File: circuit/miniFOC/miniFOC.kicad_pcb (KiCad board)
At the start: 2 copper layers, 68 parts, among them J1 Conn_01x05, J2 Conn_01x06, J3 Conn_01x02, J4 Conn_01x01, J5 Conn_01x01, J6 Conn_01x01, Q1 AP30H50Q, Q2 AP30H50Q, Q3 AP30H50Q, Q4 AP30H50Q, Q5 AP30H50Q, Q6 AP30H50Q, U1 XC6206P332MR, U2 AT32F421C8, U3 LM321, U4 COS722MR, U5 EG2133, U6 JW5017S

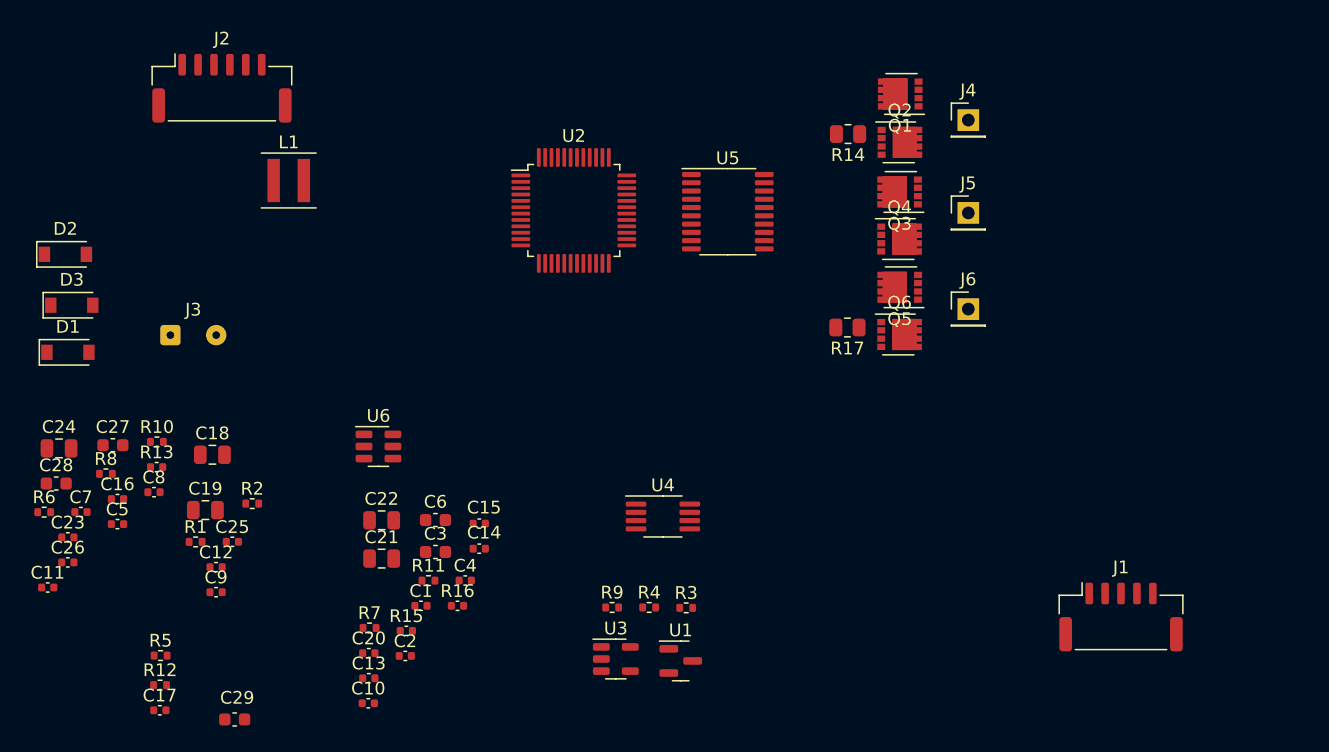
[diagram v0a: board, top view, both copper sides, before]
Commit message: Complete the circuit and PCB design for version 2.0.
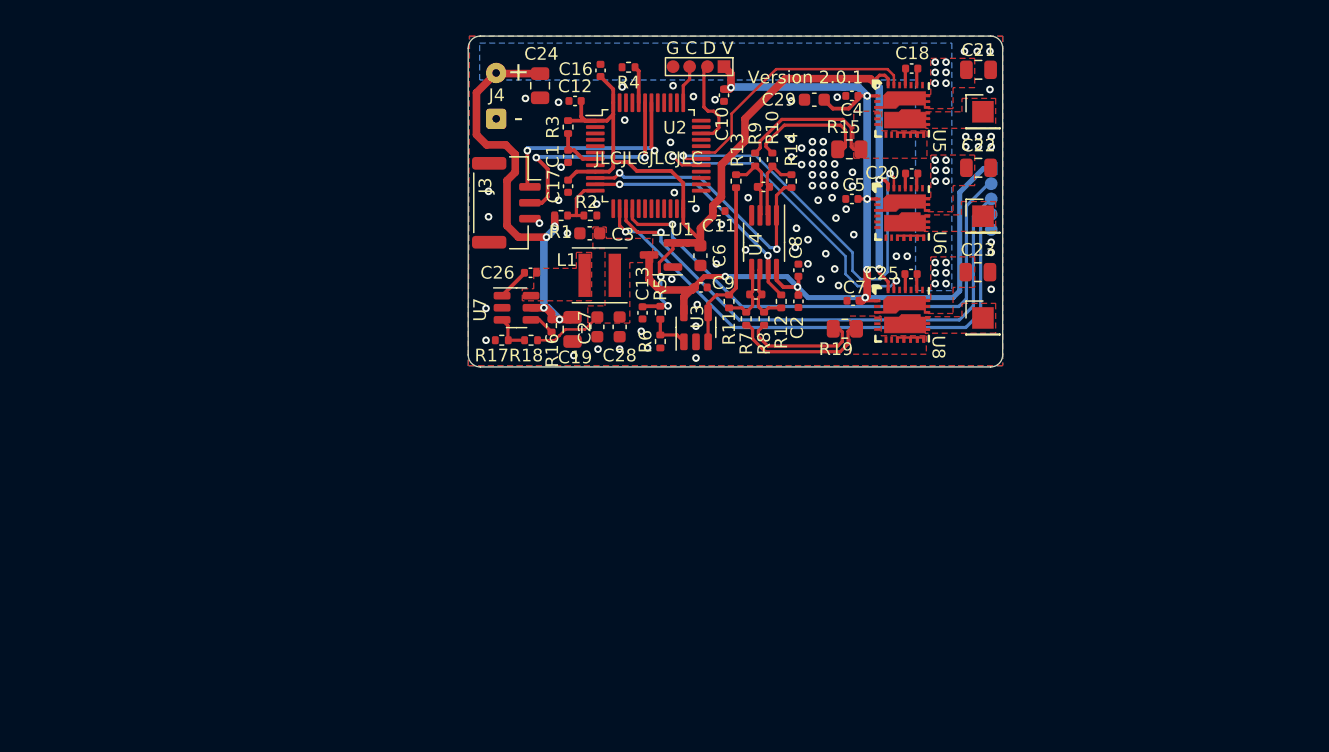
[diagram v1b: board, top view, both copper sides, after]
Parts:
- removed the C23 at (101.2, 131.0)
- removed D1, D2, D3: B0530W, Diode_SMD:D_SOD-123
- removed Q1, Q2, Q3, Q4, Q5, Q6: AP30H50Q, Package_SON:VSON-8_3.3x3.3mm_P0.65mm_NexFET
- added C20: 1uF, Library:C_0402_1005Metric, F.Cu at (167.6, 102.4)
- added G***: LOGO, Library:LOGO, B.Cu at (139.2, 106.3)
- added J3: Conn_01x03, Library:JST_GH_SM03B-GHS-TB_1x03-1MP_P1.25mm_Horizontal, F.Cu at (135.7, 104.7)
- added R1: 1kR, Library:R_0402_1005Metric, F.Cu at (140.0, 105.7)
- added R2: 1kR, Library:R_0402_1005Metric, F.Cu at (142.3, 105.7)
- added U6: uP9636, Library:QFN-26_4040_IPS, F.Cu at (166.8, 105.5)
- added U8: uP9636, Library:QFN-26_4040_IPS, F.Cu at (166.8, 113.5)
- C1, C10, C11, C12, C13, C14, C15, C16, C17, C2, C25, C26, C4, C5, C7, C8, C9: footprint Capacitor_SMD:C_0402_1005Metric -> Library:C_0402_1005Metric
- C18: renamed from C20; footprint Capacitor_SMD:C_0402_1005Metric -> Library:C_0402_1005Metric
- C19: renamed from C18; footprint Capacitor_SMD:C_0805_2012Metric -> Library:C_0805_2012Metric
- C21: renamed from C19; footprint Capacitor_SMD:C_0805_2012Metric -> Library:C_0805_2012Metric
- C22: renamed from C21; footprint Capacitor_SMD:C_0805_2012Metric -> Library:C_0805_2012Metric
- C23: renamed from C22; footprint Capacitor_SMD:C_0805_2012Metric -> Library:C_0805_2012Metric
- C24: footprint Capacitor_SMD:C_0805_2012Metric -> Library:C_0805_2012Metric
- C27, C28, C29: footprint Capacitor_SMD:C_0603_1608Metric -> Library:C_0603_1608Metric
- C3, C6: value 10uF -> 22uF; footprint Capacitor_SMD:C_0603_1608Metric -> Library:C_0603_1608Metric
- J1: footprint Connector_JST:JST_GH_SM05B-GHS-TB_1x05-1MP_P1.25mm_Horizontal -> Library:Pad_5; moved to B.Cu
- J2: value Conn_01x06 -> Conn_01x04; footprint Connector_JST:JST_GH_SM06B-GHS-TB_1x06-1MP_P1.25mm_Horizontal -> Library:Pad_4
- J4: renamed from J3; footprint Connector_Wire:SolderWire-0.1sqmm_1x02_P3.6mm_D0.4mm_OD1mm -> Library:SolderWire-0.1sqmm_1x02_P3.6mm_D0.4mm_OD1mm
- J5: renamed from J4; footprint Connector_PinHeader_2.54mm:PinHeader_1x01_P2.54mm_Vertical -> Library:Pad_1
- J6: renamed from J5; footprint Connector_PinHeader_2.54mm:PinHeader_1x01_P2.54mm_Vertical -> Library:Pad_1
- J7: renamed from J6; footprint Connector_PinHeader_2.54mm:PinHeader_1x01_P2.54mm_Vertical -> Library:Pad_1
- L1: footprint Inductor_SMD:L_Coilcraft_XxL4040 -> Library:L_Coilcraft_XxL4040
- R10: renamed from R8; footprint Resistor_SMD:R_0402_1005Metric -> Library:R_0402_1005Metric
- R11: renamed from R9; footprint Resistor_SMD:R_0402_1005Metric -> Library:R_0402_1005Metric
- R12: renamed from R10; footprint Resistor_SMD:R_0402_1005Metric -> Library:R_0402_1005Metric
- R13: renamed from R11; footprint Resistor_SMD:R_0402_1005Metric -> Library:R_0402_1005Metric
- R14: renamed from R12; footprint Resistor_SMD:R_0402_1005Metric -> Library:R_0402_1005Metric
- R15: renamed from R14; footprint Resistor_SMD:R_0805_2012Metric -> Library:R_0805_2012Metric
- R16: renamed from R13; footprint Capacitor_SMD:C_0402_1005Metric -> Library:R_0402_1005Metric
- R17: renamed from R15; footprint Capacitor_SMD:C_0402_1005Metric -> Library:R_0402_1005Metric
- R18: renamed from R16; footprint Capacitor_SMD:C_0402_1005Metric -> Library:R_0402_1005Metric
- R19: renamed from R17; footprint Resistor_SMD:R_0805_2012Metric -> Library:R_0805_2012Metric
- R3: renamed from R1; footprint Resistor_SMD:R_0402_1005Metric -> Library:R_0402_1005Metric
- R4: renamed from R2; footprint Resistor_SMD:R_0402_1005Metric -> Library:R_0402_1005Metric
- R5: renamed from R3; footprint Resistor_SMD:R_0402_1005Metric -> Library:R_0402_1005Metric
- R6: renamed from R4; footprint Resistor_SMD:R_0402_1005Metric -> Library:R_0402_1005Metric
- R7: renamed from R5; footprint Resistor_SMD:R_0402_1005Metric -> Library:R_0402_1005Metric
- R8: renamed from R6; footprint Resistor_SMD:R_0402_1005Metric -> Library:R_0402_1005Metric
- R9: renamed from R7; footprint Resistor_SMD:R_0402_1005Metric -> Library:R_0402_1005Metric
- U1: footprint Package_TO_SOT_SMD:SOT-23 -> Library:SOT-23
- U2: footprint Package_QFP:LQFP-48_7x7mm_P0.5mm -> Library:LQFP-48_7x7mm_P0.5mm
- U3: footprint Package_TO_SOT_SMD:SOT-23-5 -> Library:SOT-23-5
- U4: footprint Package_SO:MSOP-8_3x3mm_P0.65mm -> Library:MSOP-8_3x3mm_P0.65mm
- U5: value EG2133 -> uP9636; footprint Package_SO:TSSOP-20_4.4x6.5mm_P0.65mm -> Library:QFN-26_4040_IPS
- U7: renamed from U6; footprint Package_TO_SOT_SMD:SOT-23-6 -> Library:SOT-23-6
- moved C21 69.9 mm to (172.8, 94.2), turned to 180 degrees
- moved C29 66.7 mm to (159.9, 96.6)
- moved R14 63.5 mm to (158.1, 103.0), turned to -90 degrees
- moved C5 63.1 mm to (162.8, 104.4), turned to 180 degrees
- moved C7 62.9 mm to (162.9, 112.4), turned to 180 degrees
- moved C18 62.7 mm to (167.6, 94.2)
- moved C11 60.5 mm to (152.4, 105.3)
- moved R8 58.6 mm to (155.9, 113.8), turned to -90 degrees
- moved R10 57.9 mm to (156.6, 101.3), turned to 90 degrees
- moved C25 57.3 mm to (167.5, 110.3)
- moved C22 56.1 mm to (172.8, 102.0), turned to 180 degrees
- moved C10 55.4 mm to (152.8, 96.2), turned to -90 degrees
- moved C8 53.6 mm to (158.7, 110.0), turned to 90 degrees
- moved R7 53.1 mm to (154.6, 113.8), turned to 90 degrees
- moved C17 52.2 mm to (140.6, 103.4), turned to -90 degrees
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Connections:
- C18 pad 1: /VB1 -> Net-(C18-Pad1)
- C18 pad 2: /VS1 -> Net-(C18-Pad2)
- C25 pad 1: /VB3 -> Net-(C25-Pad1)
- C25 pad 2: /VS3 -> Net-(C25-Pad2)
- J2 pad 2: /USART1_TX -> /SWDIO
- J2 pad 3: /USART1_RX -> /SWDCLK
- J2 pad 4: /SWDIO -> GND
- J5 pad 1: /VS1 -> Net-(J5-Pad1)
- J6 pad 1: /VS2 -> Net-(J6-Pad1)
- J7 pad 1: /VS3 -> Net-(J7-Pad1)
- U5 pad 1: /TIM1_CH3 -> +5V
- U5 pad 2: /TIM1_CH2 -> unconnected-(U5-Pad2)
- U5 pad 20: /VB1 -> unconnected-(U5-Pad20)
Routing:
- net +5V: track 0.00 -> 90.1 mm, vias 0 -> 7
- net +3.3V: track 0.00 -> 82.5 mm, vias 0 -> 5
- net /SPI_CS: track 0.00 -> 41.6 mm, vias 0 -> 1
- net /SPI_CLK: track 0.00 -> 41.4 mm, vias 0 -> 1
- net /SPI_MISO: track 0.00 -> 40.7 mm, vias 0 -> 1
- net +15V: track 0.00 -> 35.2 mm, vias 0 -> 22
- net /TIM1_CH2: track 0.00 -> 31.8 mm, vias 0 -> 2
- net /TIM1_CH1: track 0.00 -> 26.1 mm, vias 0 -> 2
- net /ADC1_CH0: track 0.00 -> 22.6 mm, vias 0 -> 2
- net /TIM1_CH3: track 0.00 -> 19.8 mm
- net GND: track 0.00 -> 19.7 mm, vias 0 -> 81
- net /ADC1_CH1: track 0.00 -> 19.4 mm, vias 0 -> 2
- net /USART1_RX: track 0.00 -> 18.0 mm, vias 0 -> 2
- net /USART1_TX: track 0.00 -> 17.1 mm, vias 0 -> 2
- net VAA: track 0.00 -> 13.6 mm
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- added copper zone on B.Cu, net +15V
- added copper zone on F.Cu, net +15V
- added copper zone on F.Cu, net +5V
- added copper zone on F.Cu, net /SA1_P
- added copper zone on F.Cu, net /SA2_P
- added copper zone on B.Cu, net GND
- added copper zone on F.Cu, net GND
- added copper zone on F.Cu, net Net-(C26-Pad1)
- added copper zone on F.Cu, net Net-(J5-Pad1)
- added copper zone on F.Cu, net Net-(J6-Pad1)
- added copper zone on F.Cu, net Net-(J7-Pad1)
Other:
- board outline added: 42 x 26 mm
- board text added: "+"
- board text added: "-"
- board text added: "0"
- board text added: "0 mm"
- board text added: "0.01 mm"
- board text added: "0.02"
- board text added: "0.035 mm"
- board text added: "0.2000 mm / 0.2000 mm"
- board text added: "0.3000 mm"
- board text added: "1"
- board text added: "1.51 mm"
- board text added: "1.6000 mm"
- board text added: "2"
- board text added: "3.3"
- board text added: "4.5"
- board text added: "42.0000 mm x 26.0000 mm"
- board text added: "B.Cu"
- board text added: "B.Mask"
- board text added: "B.Paste"
- board text added: "B.Silkscreen"
- board text added: "BOARD CHARACTERISTICS"
- board text added: "Black"
- board text added: "Bottom Silk Screen"
- board text added: "Bottom Solder Mask"
- board text added: "Bottom Solder Paste"
- board text added: "Epsilon R（相对介电常数）"
- board text added: "F.Cu"
- board text added: "F.Mask"
- board text added: "F.Paste"
- board text added: "F.Silkscreen"
- board text added: "FR4"
- board text added: "G C D V"
- board text added: "JLCJLCJLCJLC"
- board text added: "Loss Tangent（损耗角正切）"
- board text added: "None"
- board text added: "Not specified"
- board text added: "Top Silk Screen"
- board text added: "Top Solder Mask"
- board text added: "Top Solder Paste"
- board text added: "V I C E G"
- board text added: "Version 2.0.1"
- board text added: "White"
- board text added: "copper"
- board text added: "core"
- board text added: "github.com/zhuyanzhen1/miniFOC"
- board text added: "miniFOC"
- board text added: "否"
- board text added: "孔最小直径："
- board text added: "层名称"
- board text added: "最小布线/间距："
- board text added: "材料"
- board text added: "板子整体尺寸："
- board text added: "电介质层 1"
- board text added: "电路板厚度："
- board text added: "电镀板边："
- board text added: "类型"
- board text added: "粗细 (mm)"
- board text added: "边缘卡连接器："
- board text added: "邮票孔："
- board text added: "铜层数量："
- board text added: "铜表面处理（镀铜）："
- board text added: "阻抗控制"
- board text added: "颜色"

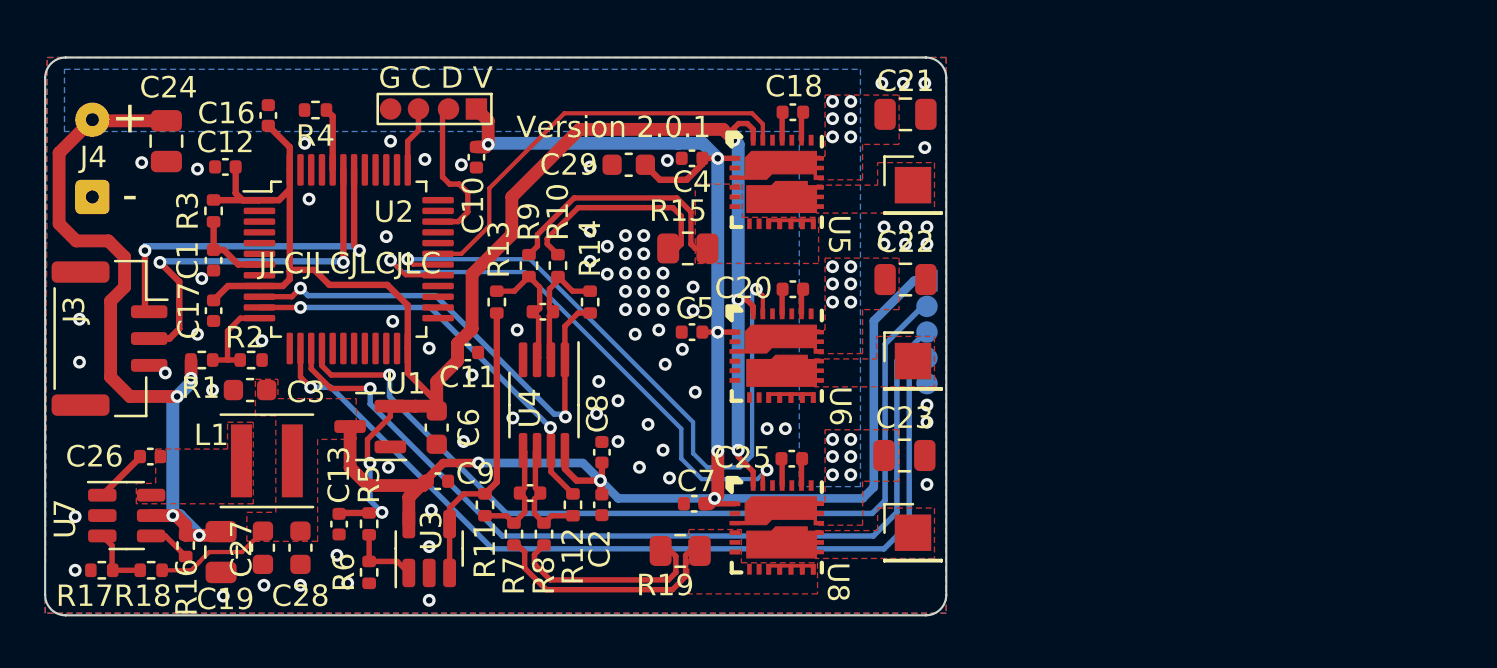
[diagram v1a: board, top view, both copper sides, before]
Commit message: Mosify miniFOC schematic, using new scheme
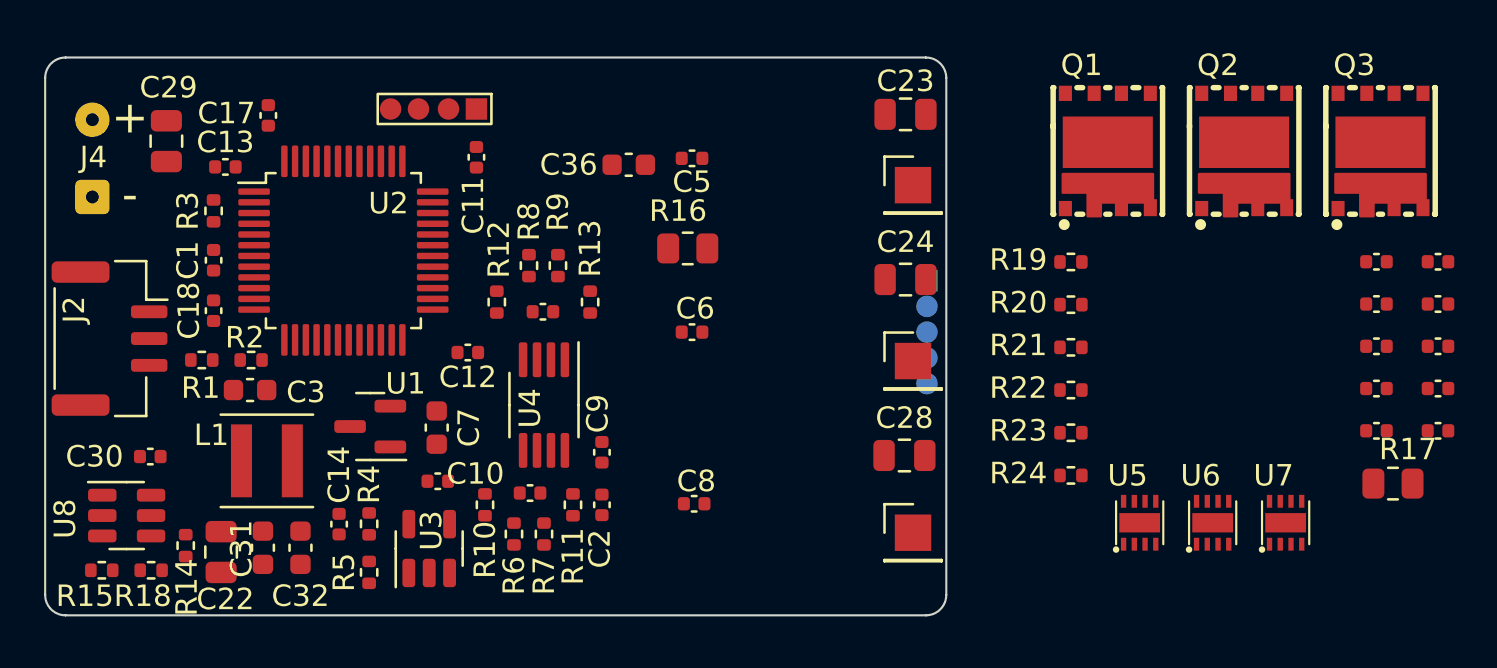
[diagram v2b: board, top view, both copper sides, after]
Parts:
- removed the C18 at (167.6, 94.2)
- removed G***: LOGO, Library:LOGO
- removed the R4 at (145.3, 94.0)
- removed the U8 at (166.8, 113.5)
- added C19: 100nF, library:C_0402_1005Metric, F.Cu at (194.8, 103.1)
- added C21: 100nF, library:C_0402_1005Metric, F.Cu at (194.8, 107.0)
- added C26: 1uF, library:C_0402_1005Metric, F.Cu at (197.6, 101.1)
- added C27: 1uF, library:C_0402_1005Metric, F.Cu at (197.6, 103.1)
- added C33: 1uF, library:C_0402_1005Metric, F.Cu at (197.6, 105.1)
- added C34: 1uF, library:C_0402_1005Metric, F.Cu at (197.6, 107.0)
- added C35: 1uF, library:C_0402_1005Metric, F.Cu at (197.6, 109.0)
- added C4: 1uF, library:C_0402_1005Metric, F.Cu at (194.8, 101.1)
- added Q1: RU30J30M, library:PDFN-8_L5.8-W4.9_RU30J30M, F.Cu at (182.2, 96.0)
- added Q2: RU30J30M, library:PDFN-8_L5.8-W4.9_RU30J30M, F.Cu at (188.6, 96.0)
- added Q3: RU30J30M, library:PDFN-8_L5.8-W4.9_RU30J30M, F.Cu at (194.9, 96.0)
- added R17: 20mR, library:R_0805_2012Metric, F.Cu at (195.5, 111.5)
- added R20: 1kR, library:R_0402_1005Metric, F.Cu at (180.5, 103.1)
- added R21: 10kR, library:R_0402_1005Metric, F.Cu at (180.5, 105.1)
- added R22: 1kR, library:R_0402_1005Metric, F.Cu at (180.5, 107.1)
- added R23: 10kR, library:R_0402_1005Metric, F.Cu at (180.5, 109.1)
- added R24: 1kR, library:R_0402_1005Metric, F.Cu at (180.5, 111.1)
- added U7: BDR2L00, library:TDFN-8_L2.0-W2.0-P0.50-BL-EP, F.Cu at (190.5, 113.3)
- C1, C2, C25: footprint Library:C_0402_1005Metric -> library:C_0402_1005Metric
- C10: renamed from C9; footprint Library:C_0402_1005Metric -> library:C_0402_1005Metric
- C11: renamed from C10; footprint Library:C_0402_1005Metric -> library:C_0402_1005Metric
- C12: renamed from C11; footprint Library:C_0402_1005Metric -> library:C_0402_1005Metric
- C13: renamed from C12; footprint Library:C_0402_1005Metric -> library:C_0402_1005Metric
- C14: renamed from C13; footprint Library:C_0402_1005Metric -> library:C_0402_1005Metric
- C15: renamed from C14; footprint Library:C_0402_1005Metric -> library:C_0402_1005Metric
- C16: renamed from C15; footprint Library:C_0402_1005Metric -> library:C_0402_1005Metric
- C17: renamed from C16; footprint Library:C_0402_1005Metric -> library:C_0402_1005Metric
- C18: renamed from C17; footprint Library:C_0402_1005Metric -> library:C_0402_1005Metric
- C20: value 1uF -> 100nF; footprint Library:C_0402_1005Metric -> library:C_0402_1005Metric
- C22: renamed from C19; footprint Library:C_0805_2012Metric -> library:C_0805_2012Metric
- C23: renamed from C21; footprint Library:C_0805_2012Metric -> library:C_0805_2012Metric
- C24: renamed from C22; footprint Library:C_0805_2012Metric -> library:C_0805_2012Metric
- C28: renamed from C23; footprint Library:C_0805_2012Metric -> library:C_0805_2012Metric
- C29: renamed from C24; footprint Library:C_0805_2012Metric -> library:C_0805_2012Metric
- C3: footprint Library:C_0603_1608Metric -> library:C_0603_1608Metric
- C30: renamed from C26; footprint Library:C_0402_1005Metric -> library:C_0402_1005Metric
- C31: renamed from C27; footprint Library:C_0603_1608Metric -> library:C_0603_1608Metric
- C32: renamed from C28; footprint Library:C_0603_1608Metric -> library:C_0603_1608Metric
- C36: renamed from C29; footprint Library:C_0603_1608Metric -> library:C_0603_1608Metric
- C5: renamed from C4; footprint Library:C_0402_1005Metric -> library:C_0402_1005Metric
- C6: renamed from C5; footprint Library:C_0402_1005Metric -> library:C_0402_1005Metric
- C7: renamed from C6; footprint Library:C_0603_1608Metric -> library:C_0603_1608Metric
- C8: renamed from C7; footprint Library:C_0402_1005Metric -> library:C_0402_1005Metric
- C9: renamed from C8; footprint Library:C_0402_1005Metric -> library:C_0402_1005Metric
- J1: footprint Library:Pad_5 -> library:Pad_5
- J2: renamed from J3; footprint Library:JST_GH_SM03B-GHS-TB_1x03-1MP_P1.25mm_Horizontal -> library:JST_GH_SM03B-GHS-TB_1x03-1MP_P1.25mm_Horizontal
- J3: renamed from J2; footprint Library:Pad_4 -> library:Pad_4
- J4: footprint Library:SolderWire-0.1sqmm_1x02_P3.6mm_D0.4mm_OD1mm -> library:SolderWire-0.1sqmm_1x02_P3.6mm_D0.4mm_OD1mm
- J5, J6, J7: footprint Library:Pad_1 -> library:Pad_1
- L1: footprint Library:L_Coilcraft_XxL4040 -> library:L_Coilcraft_XxL4040
- R1: value 1kR -> 10kR; footprint Library:R_0402_1005Metric -> library:R_0402_1005Metric
- R10: renamed from R11; footprint Library:R_0402_1005Metric -> library:R_0402_1005Metric
- R11: renamed from R12; footprint Library:R_0402_1005Metric -> library:R_0402_1005Metric
- R12: renamed from R13; footprint Library:R_0402_1005Metric -> library:R_0402_1005Metric
- R13: renamed from R14; footprint Library:R_0402_1005Metric -> library:R_0402_1005Metric
- R14: renamed from R16; footprint Library:R_0402_1005Metric -> library:R_0402_1005Metric
- R15: renamed from R17; footprint Library:R_0402_1005Metric -> library:R_0402_1005Metric
- R16: renamed from R15; footprint Library:R_0805_2012Metric -> library:R_0805_2012Metric
- R18, R2, R3: footprint Library:R_0402_1005Metric -> library:R_0402_1005Metric
- R19: value 20mR -> 10kR; footprint Library:R_0805_2012Metric -> library:R_0402_1005Metric
- R4: renamed from R5; footprint Library:R_0402_1005Metric -> library:R_0402_1005Metric
- R5: renamed from R6; footprint Library:R_0402_1005Metric -> library:R_0402_1005Metric
- R6: renamed from R7; footprint Library:R_0402_1005Metric -> library:R_0402_1005Metric
- R7: renamed from R8; footprint Library:R_0402_1005Metric -> library:R_0402_1005Metric
- R8: renamed from R9; footprint Library:R_0402_1005Metric -> library:R_0402_1005Metric
- R9: renamed from R10; footprint Library:R_0402_1005Metric -> library:R_0402_1005Metric
- U1: footprint Library:SOT-23 -> library:SOT-23
- U2: value AT32F421C8 -> CH32V203C8T6; footprint Library:LQFP-48_7x7mm_P0.5mm -> library:LQFP-48_7x7mm_P0.5mm
- U3: footprint Library:SOT-23-5 -> library:SOT-23-5
- U4: footprint Library:MSOP-8_3x3mm_P0.65mm -> library:MSOP-8_3x3mm_P0.65mm
- U5, U6: value uP9636 -> BDR2L00; footprint Library:QFN-26_4040_IPS -> library:TDFN-8_L2.0-W2.0-P0.50-BL-EP
- U8: renamed from U7; footprint Library:SOT-23-6 -> library:SOT-23-6
- moved C20 27.3 mm to (194.8, 105.1)
- moved C25 27.3 mm to (194.8, 109.0)
- moved U5 23.2 mm to (183.7, 113.3), turned to 0 degrees
- moved R19 22.7 mm to (180.5, 101.1), turned to 0 degrees
- moved U6 21.8 mm to (187.1, 113.3), turned to 0 degrees
- moved U2 0.47 mm to (146.6, 100.6)
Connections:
- C20 pad 1: Net-(C20-Pad1) -> +5V
- C20 pad 2: Net-(C20-Pad2) -> GND
- C25 pad 1: Net-(C25-Pad1) -> Net-(U5-BOOT)
- C25 pad 2: Net-(C25-Pad2) -> /PHASE1
- J5 pad 1: Net-(J5-Pad1) -> /PHASE1
- J6 pad 1: Net-(J6-Pad1) -> /PHASE2
- J7 pad 1: Net-(J7-Pad1) -> /PHASE3
- R19 pad 1: /SA2_P -> /PHASE1
- R19 pad 2: GND -> /ADC_U
- U2 pad 13: unconnected-(U2-Pad13) -> /ADC_U
- U2 pad 14: /SPI_CS -> /ADC_V
- U2 pad 15: /SPI_CLK -> /ADC_W
- U2 pad 16: /SPI_MISO -> unconnected-(U2-PA6-Pad16)
- U2 pad 25: unconnected-(U2-Pad25) -> /SPI_CS
- U2 pad 26: unconnected-(U2-Pad26) -> /SPI_CLK
- U2 pad 27: unconnected-(U2-Pad27) -> /SPI_MISO
- U2 pad 44: /BOOT0 -> GND
- U5 pad 1: +5V -> Net-(U5-BOOT)
- U5 pad 2: unconnected-(U5-Pad2) -> /TIM1_CH1
- U6 pad 1: +5V -> Net-(U6-BOOT)
- U6 pad 2: unconnected-(U6-Pad2) -> /TIM1_CH2
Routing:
- net +5V: track 90.1 -> 0.00 mm, vias 7 -> 0
- net +3.3V: track 82.5 -> 0.00 mm, vias 5 -> 0
- net /SPI_CS: track 41.6 -> 0.00 mm, vias 1 -> 0
- net /SPI_CLK: track 41.4 -> 0.00 mm, vias 1 -> 0
- net /SPI_MISO: track 40.7 -> 0.00 mm, vias 1 -> 0
- net +15V: track 35.2 -> 0.00 mm, vias 22 -> 0
- net /TIM1_CH2: track 31.8 -> 0.00 mm, vias 2 -> 0
- net /TIM1_CH1: track 26.1 -> 0.00 mm, vias 2 -> 0
- net /ADC1_CH0: track 22.6 -> 0.00 mm, vias 2 -> 0
- net /TIM1_CH3: track 19.8 -> 0.00 mm
- net GND: track 19.7 -> 0.00 mm, vias 81 -> 0
- net /ADC1_CH1: track 19.4 -> 0.00 mm, vias 2 -> 0
- net /USART1_RX: track 18.0 -> 0.00 mm, vias 2 -> 0
- net /USART1_TX: track 17.1 -> 0.00 mm, vias 2 -> 0
- net VAA: track 13.6 -> 0.00 mm
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- removed copper zone on B.Cu, net +15V
- removed copper zone on F.Cu, net +15V
- removed copper zone on F.Cu, net +5V
- removed copper zone on F.Cu, net /SA1_P
- removed copper zone on F.Cu, net /SA2_P
- removed copper zone on B.Cu, net GND
- removed copper zone on F.Cu, net GND
- removed copper zone on F.Cu, net Net-(J5-Pad1)
- removed copper zone on F.Cu, net Net-(J6-Pad1)
- removed copper zone on F.Cu, net Net-(J7-Pad1)
- removed copper zone on F.Cu, net Net-(U8-SW)
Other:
- board text removed: "G C D V"
- board text removed: "JLCJLCJLCJLC"
- board text removed: "Version 2.0.1"
- board text removed: "github.com/zhuyanzhen1/miniFOC"
- board text removed: "miniFOC"
